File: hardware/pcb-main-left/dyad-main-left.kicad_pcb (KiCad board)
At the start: 2 copper layers, 149 x 120.7 mm, 129 parts, among them SW1 SW_Push, SW10 SW_Push, SW11 SW_Push, SW12 SW_Push, SW13 SW_Push, SW14 SW_Push, SW15 SW_Push, SW16 SW_Push, SW17 SW_Push, SW18 SW_Push, SW19 SW_Push, SW2 SW_Push, SW20 SW_Push, SW21 SW_Push, SW22 SW_Push, SW23 SW_Push, SW24 SW_Push, SW25 SW_Push, SW26 SW_Push, SW27 SW_Push, SW28 SW_Push, SW29 SW_Push, SW3 SW_Push, SW30 SW_Push, SW31 SW_Push, SW32 SW_Push, SW4 SW_Push, SW5 SW_Push, SW6 SW_Push, SW7 SW_Push, SW8 SW_Push, SW9 SW_Push

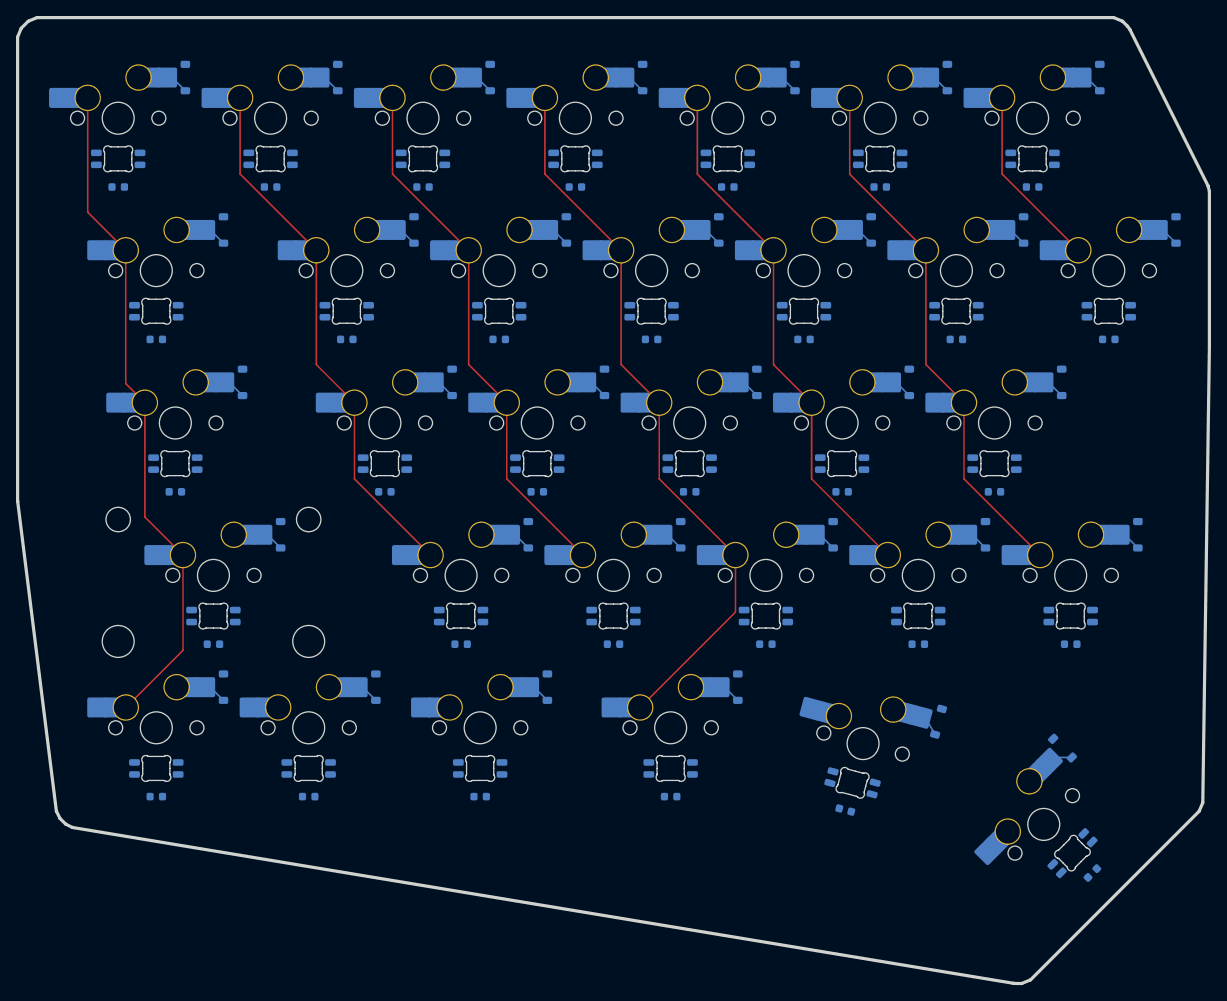
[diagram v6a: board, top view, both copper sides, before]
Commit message: Pour GND and VCC from the generator, and write down what stays manual
_add_power_pours() fills one rail per layer over the real board outline,
taken from KiCad's own outline extraction rather than reassembling the 25
Edge.Cuts segments. Pads connect solid rather than through thermal reliefs:
everything here is reflow SMD, so thermal relief buys nothing and costs the
LED rail current capacity. It also sidesteps the starved_thermal class of
error entirely.

GND goes on B.Cu, the component side. Every GND pad on these boards is
B.Cu-only, so the pour reaches all of them with no vias, and each LED's
decoupling loop to its own capacitor stays local copper rather than going
pad -> via -> plane -> via -> pad. Result: GND unconnected 0 on both halves.

VCC takes F.Cu, which carries only column traces and so gives a continuous
plane for spreading ~2 A across the LEDs. It cannot reach its pads without a
via each, and those are being added by hand -- documented rather than
generated, since via placement wants judgement about the LED/cap pairs.

  main-left    GND 12918 mm2   VCC 13646 mm2
  main-right   GND 14088 mm2   VCC 14924 mm2

Both halves regenerated, which also applies the pending bottom-row column
remap from 9b392c8. That resolved the two COL3 errors on the right -- the
0.1386 mm to LED26's cutout and 0.197 mm to SW26's NPTH pad both came from
routing that no longer exists. Every remaining error on both halves is now a
deliberate D/SW courtyard overlap.

docs/MANUAL_TASKS.md records the four things the generator cannot do: the VCC
vias, routing the rows and columns, the LED serpentine chain, and the
cosmetic silkscreen work. It carries the post-regeneration baseline numbers so
an anomaly is distinguishable from a known gap, and a "do not fix" section for
the courtyard overlaps and the 2.25u width fallback, both of which have now
been investigated twice.

Co-Authored-By: Claude Opus 5 <noreply@anthropic.com>
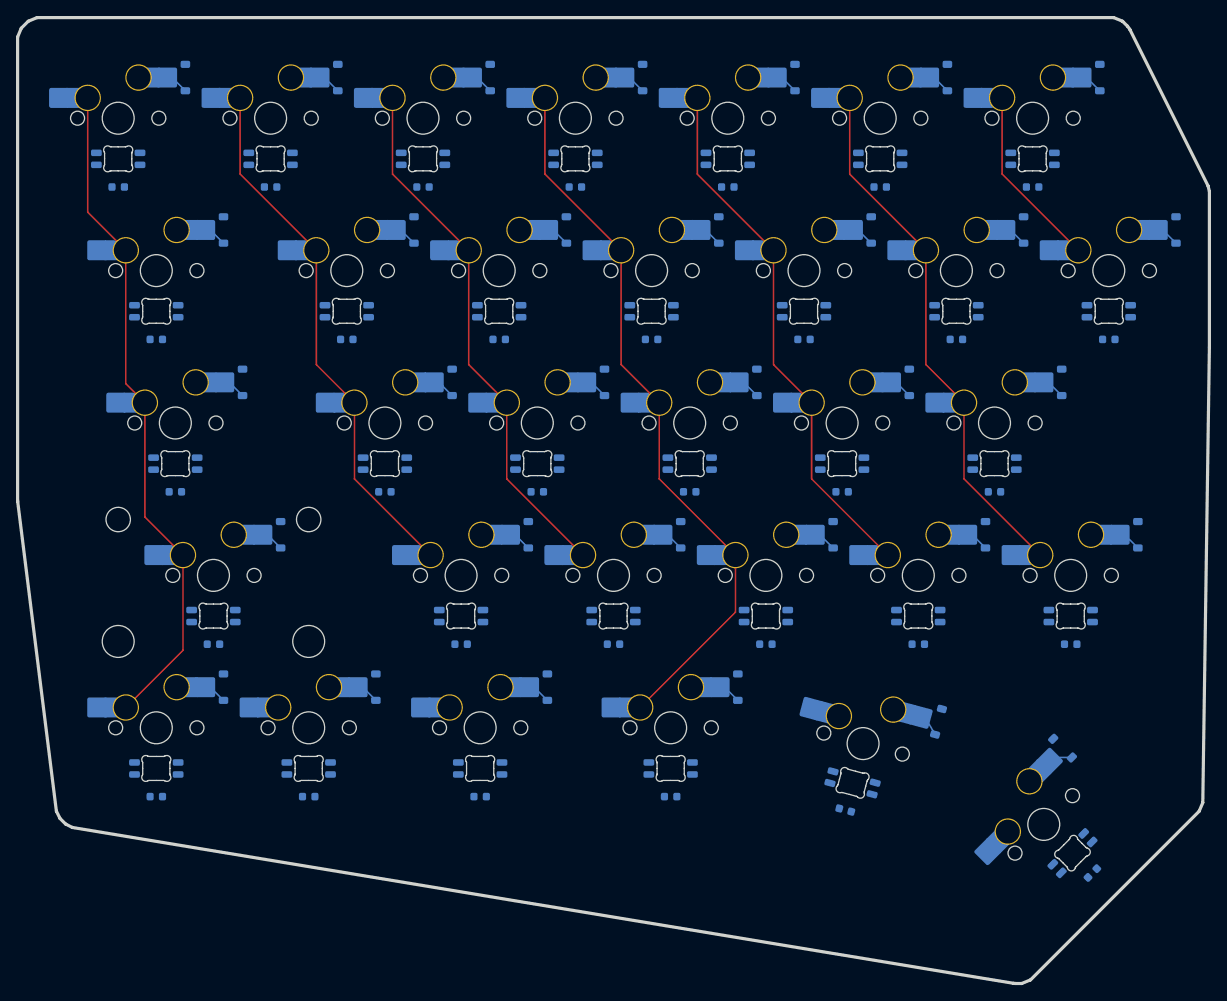
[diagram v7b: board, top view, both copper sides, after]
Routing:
- added copper zone on B.Cu, net GND
- added copper zone on F.Cu, net VCC
